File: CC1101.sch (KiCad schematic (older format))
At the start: 30 parts, among them J201 Conn_Coaxial, U201 CC1101RGPR, Y201 26MHz

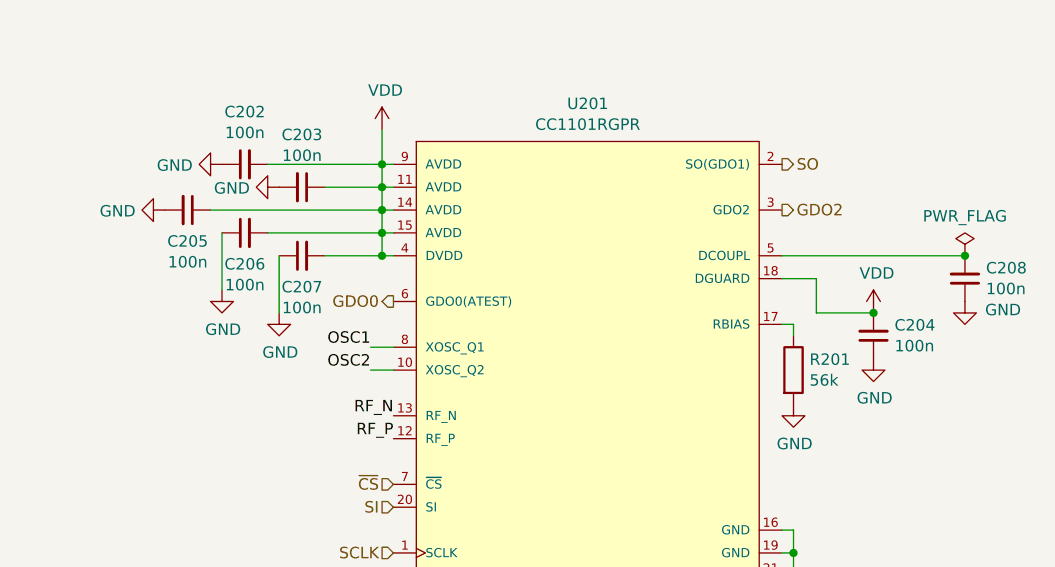
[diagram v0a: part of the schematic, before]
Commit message: select more JLC components
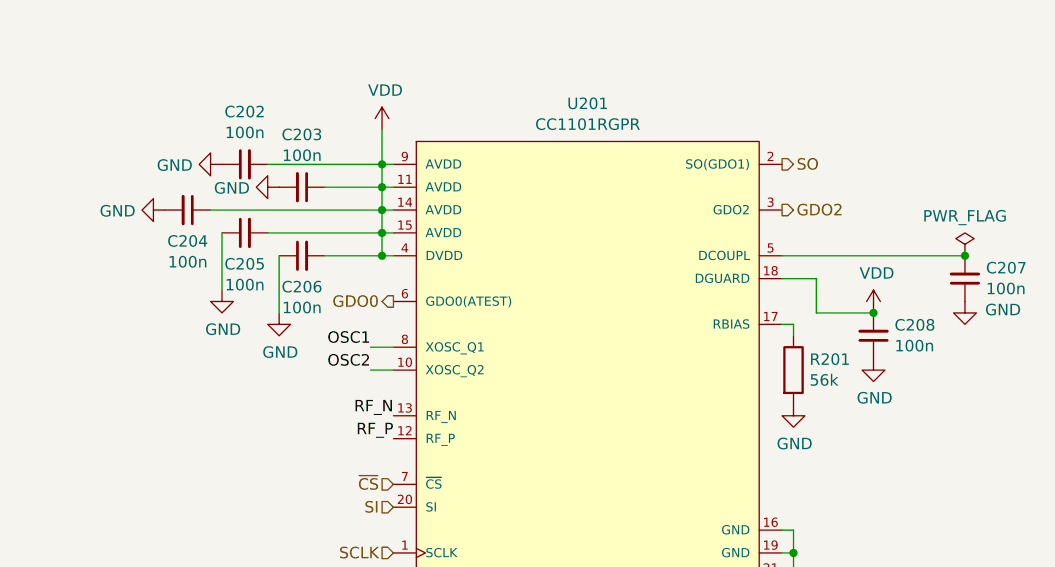
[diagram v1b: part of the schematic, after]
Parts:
- C211: LCSC (none) -> C1546; Type (none) -> FH 0402CG101J500NT
- C212, C217: LCSC (none) -> C1552; Type (none) -> FH 0402CG1R5C500NT
- C213: LCSC (none) -> C1547; Type (none) -> FH 0402CG120J500NT
- C214: footprint Capacitor_SMD:C_0402_1005Metric -> Capacitor_SMD:C_0603_1608Metric; LCSC (none) -> C1567; Type (none) -> FH 0402CG470J500NT
- C215: LCSC (none) -> C1550; Type (none) -> FH 0402CG1R0C500NT
- C216: LCSC (none) -> C1565; Type (none) -> FH 0402CG3R3C500NT
- FB201: Param Single basic one at JLC -> Only basic one at JLC
- L201, L207: LCSC (none) -> C24562; Type (none) -> Sunlord SDCL1005C18NJTDF
- L202, L203, L204, L206: LCSC (none) -> C24563; Type (none) -> Sunlord SDCL1005C12NJTDF
- renumbered C205 to C204, C206 to C205, C207 to C206, C208 to C207, C204 to C208

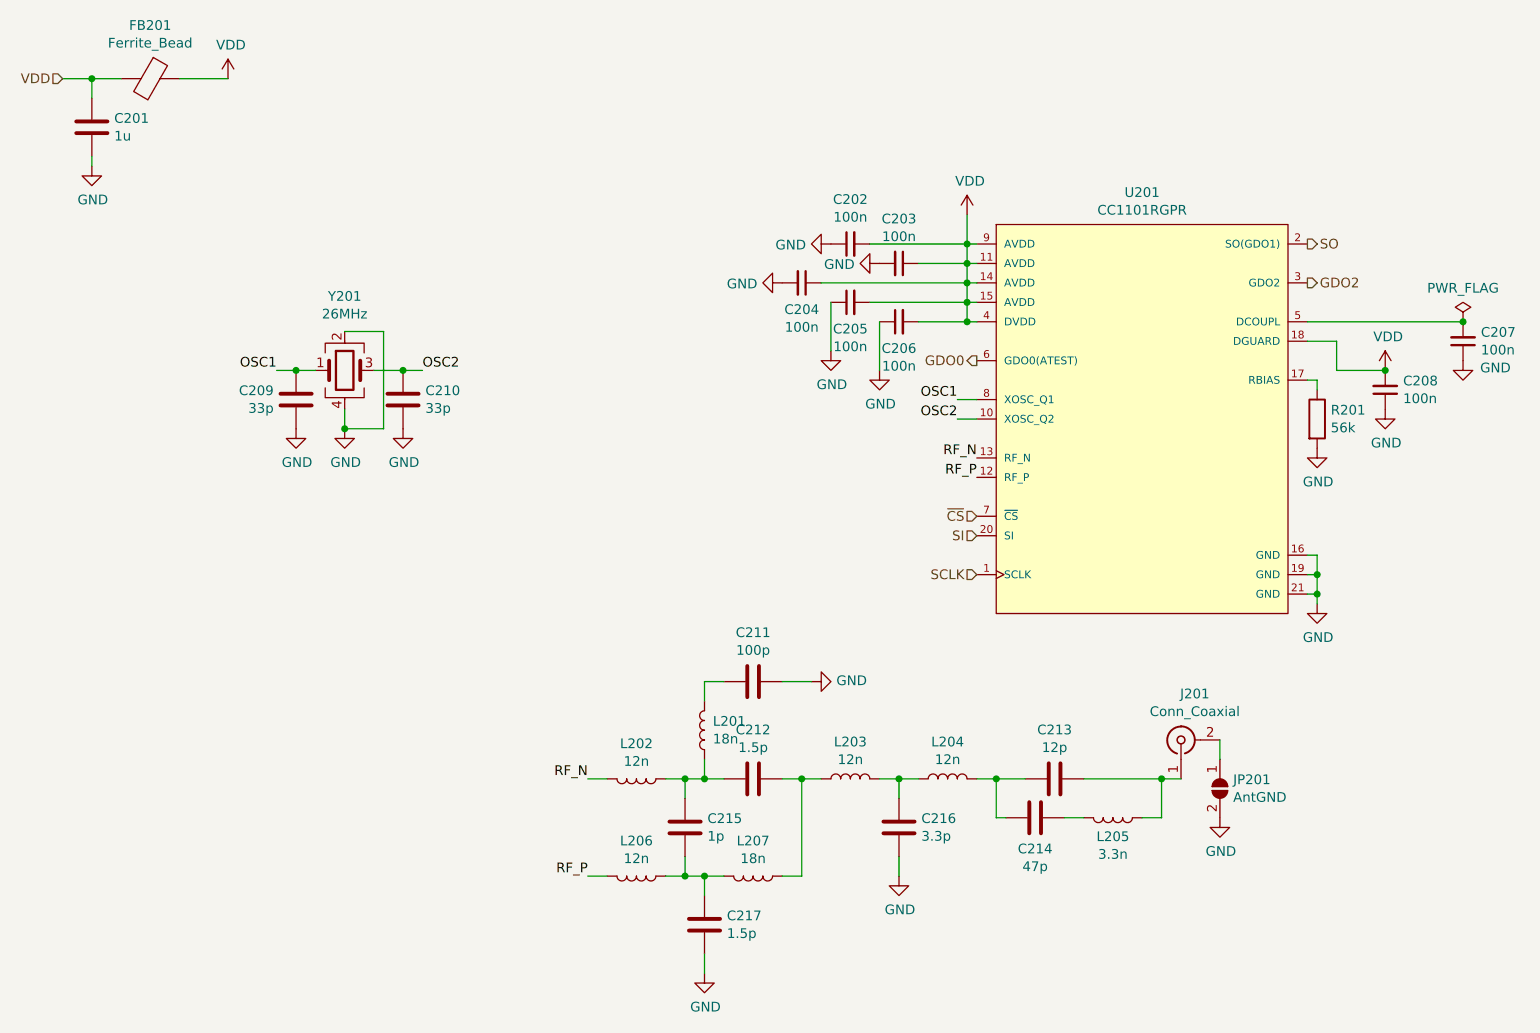
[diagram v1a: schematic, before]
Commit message: raw component placement
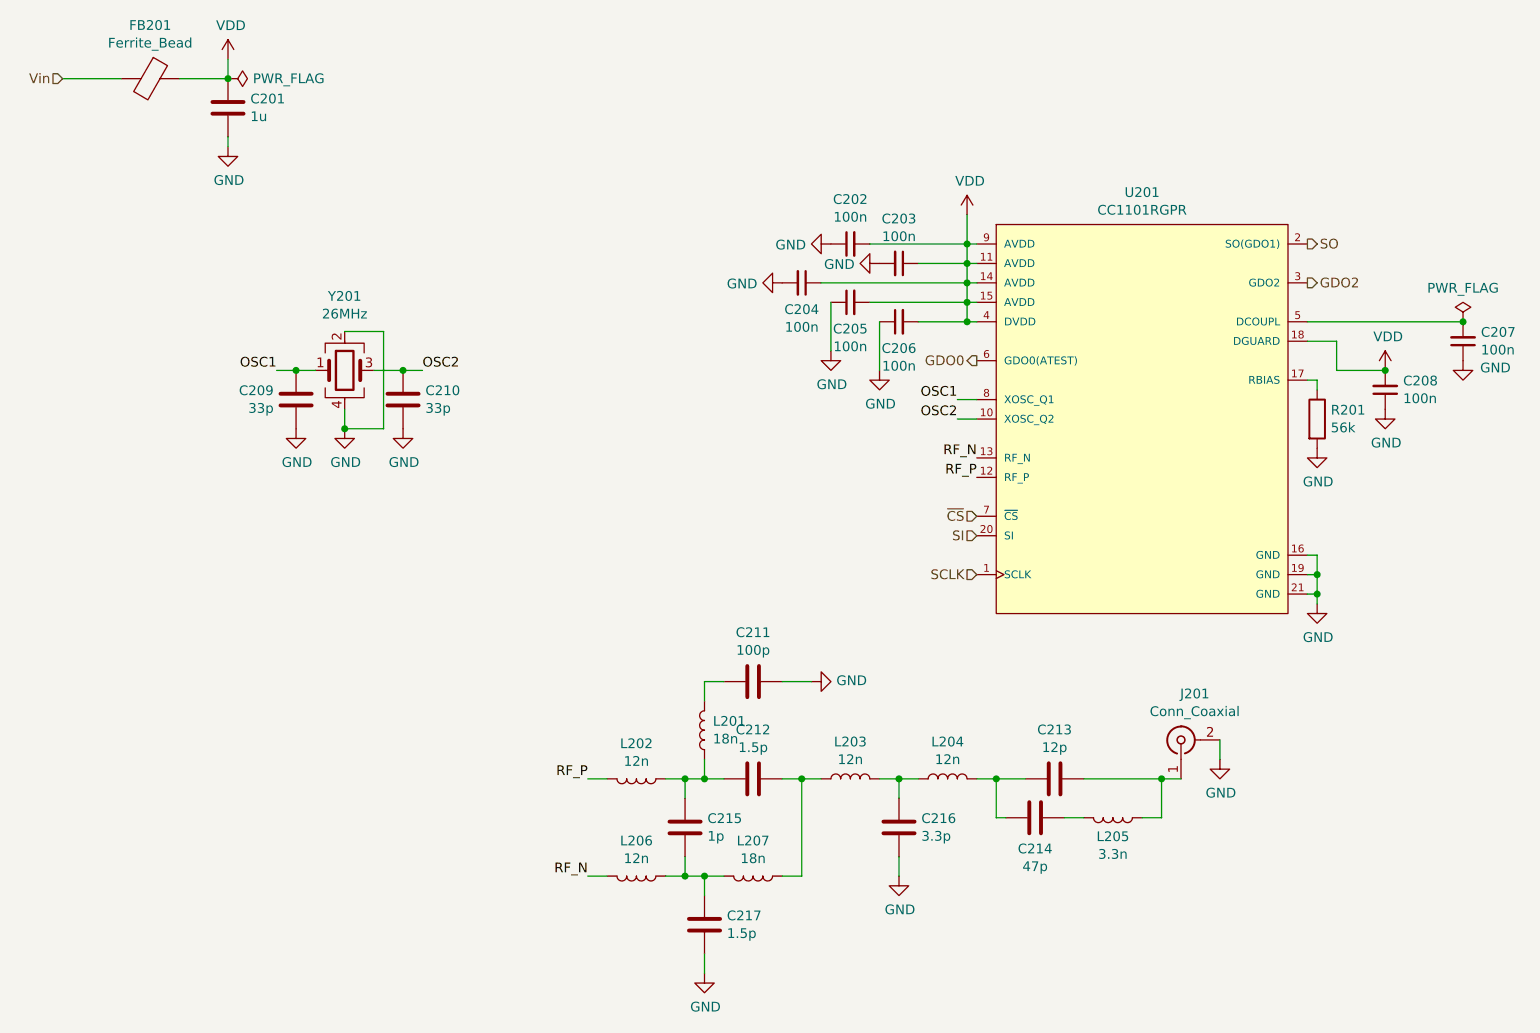
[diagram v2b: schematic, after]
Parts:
- removed JP201: AntGND, Jumper:SolderJumper-2_P1.3mm_Open_RoundedPad1.0x1.5mm, symbol Jumper:SolderJumper_2_Open
- C214: footprint Capacitor_SMD:C_0603_1608Metric -> Capacitor_SMD:C_0402_1005Metric
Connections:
- net GND: now also J201.2 (Ext)
- net RF_N: now also L206.2; no longer L202.2
- net RF_P: now also L202.2; no longer L206.2
- net VDD: no longer FB201.2
- new net Vin: FB201.2
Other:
- moved on the sheet: C201
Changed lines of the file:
@@
 GDO0
 Text HLabel 700  900  0    50   Input ~ 0
-VDD
+Vin
 $Comp
 L Device:C_Small C205
@@
 L power:VDD #PWR0201
 U 1 1 6086AF52
-P 1550 900
-F 0 "#PWR0201" H 1550 750 50  0001 C CNN
-F 1 "VDD" H 1565 1073 50  0000 C CNN
-F 2 "" H 1550 900 50  0001 C CNN
-F 3 "" H 1550 900 50  0001 C CNN
-	1    1550 900
+P 1550 800
+F 0 "#PWR0201" H 1550 650 50  0001 C CNN
+F 1 "VDD" H 1565 973 50  0000 C CNN
+F 2 "" H 1550 800 50  0001 C CNN
+F 3 "" H 1550 800 50  0001 C CNN
+	1    1550 800
 	1    0    0    -1
 $EndComp
@@
 	0    1    1    0
 $EndComp
-Wire Wire Line
-	1550 900  1300 900
 $Comp
 L Device:C C201
 U 1 1 6086D468
-P 850 1150
-F 0 "C201" H 965 1196 50  0000 L CNN
-F 1 "1u" H 965 1105 50  0000 L CNN
-F 2 "Capacitor_SMD:C_0805_2012Metric" H 888 1000 50  0001 C CNN
-F 3 "https://datasheet.lcsc.com/lcsc/1810191216_Samsung-Electro-Mechanics-CL21B105KBFNNNE_C28323.pdf" H 850 1150 50  0001 C CNN
-F 4 "Samsung CL21B105KBFNNNE" H 850 1150 50  0001 C CNN "Type"
-F 5 "C28323" H 850 1150 50  0001 C CNN "LCSC"
-F 6 "X7R" H 850 1150 50  0001 C CNN "Param"
-	1    850  1150
-	1    0    0    -1
-$EndComp
-Wire Wire Line
-	700  900  850  900
-Wire Wire Line
-	850  1000 850  900
-Connection ~ 850  900
-Wire Wire Line
-	850  900  1000 900
+P 1550 1050
+F 0 "C201" H 1665 1096 50  0000 L CNN
+F 1 "1u" H 1665 1005 50  0000 L CNN
+F 2 "Capacitor_SMD:C_0805_2012Metric" H 1588 900 50  0001 C CNN
+F 3 "https://datasheet.lcsc.com/lcsc/1810191216_Samsung-Electro-Mechanics-CL21B105KBFNNNE_C28323.pdf" H 1550 1050 50  0001 C CNN
+F 4 "Samsung CL21B105KBFNNNE" H 1550 1050 50  0001 C CNN "Type"
+F 5 "C28323" H 1550 1050 50  0001 C CNN "LCSC"
+F 6 "X7R" H 1550 1050 50  0001 C CNN "Param"
+	1    1550 1050
+	1    0    0    -1
+$EndComp
 $Comp
 L power:GND #PWR0202
 U 1 1 6086EAEC
-P 850 1350
-F 0 "#PWR0202" H 850 1100 50  0001 C CNN
-F 1 "GND" H 855 1177 50  0000 C CNN
-F 2 "" H 850 1350 50  0001 C CNN
-F 3 "" H 850 1350 50  0001 C CNN
-	1    850  1350
-	1    0    0    -1
-$EndComp
-Wire Wire Line
-	850  1350 850  1300
+P 1550 1250
+F 0 "#PWR0202" H 1550 1000 50  0001 C CNN
+F 1 "GND" H 1555 1077 50  0000 C CNN
+F 2 "" H 1550 1250 50  0001 C CNN
+F 3 "" H 1550 1250 50  0001 C CNN
+	1    1550 1250
+	1    0    0    -1
+$EndComp
+Wire Wire Line
+	1550 1250 1550 1200
+Text Label 3400 5000 2    50   ~ 0
+RF_N
 Text Label 3400 4500 2    50   ~ 0
-RF_N
-Text Label 3400 5000 2    50   ~ 0
 RF_P
 $Comp
@@
 F 0 "C214" V 5860 4700 50  0000 C CNN
 F 1 "47p" V 5951 4700 50  0000 C CNN
-F 2 "Capacitor_SMD:C_0603_1608Metric" H 5738 4550 50  0001 C CNN
+F 2 "Capacitor_SMD:C_0402_1005Metric" H 5738 4550 50  0001 C CNN
 F 3 "https://datasheet.lcsc.com/szlcsc/Guangdong-Fenghua-Advanced-Tech-0402CG470J500NT_C1567.pdf" H 5700 4700 50  0001 C CNN
 F 4 "" V 5700 4700 50  0001 C CNN "type"
@@
 	6650 4300 6650 4400
 $Comp
-L power:GND #PWR0218
-U 1 1 608ABD9C
-P 6650 4700
-F 0 "#PWR0218" H 6650 4450 50  0001 C CNN
-F 1 "GND" H 6655 4527 50  0000 C CNN
-F 2 "" H 6650 4700 50  0001 C CNN
-F 3 "" H 6650 4700 50  0001 C CNN
-	1    6650 4700
-	1    0    0    -1
-$EndComp
-$Comp
-L Jumper:SolderJumper_2_Open JP201
-U 1 1 608E6674
-P 6650 4550
-F 0 "JP201" V 6604 4618 50  0000 L CNN
-F 1 "AntGND" V 6695 4618 50  0000 L CNN
-F 2 "Jumper:SolderJumper-2_P1.3mm_Open_RoundedPad1.0x1.5mm" H 6650 4550 50  0001 C CNN
-F 3 "~" H 6650 4550 50  0001 C CNN
-F 4 "0" H 6650 4550 50  0001 C CNN "JLCPCB BOM"
-	1    6650 4550
-	0    1    1    0
-$EndComp
-$Comp
 L power:GND #PWR0220
 U 1 1 608E70BF
@@
 	7250 2400 7500 2400
 Connection ~ 7500 2400
+$Comp
+L power:GND #PWR0218
+U 1 1 608ABD9C
+P 6650 4400
+F 0 "#PWR0218" H 6650 4150 50  0001 C CNN
+F 1 "GND" H 6655 4227 50  0000 C CNN
+F 2 "" H 6650 4400 50  0001 C CNN
+F 3 "" H 6650 4400 50  0001 C CNN
+	1    6650 4400
+	1    0    0    -1
+$EndComp
+Wire Wire Line
+	700  900  1000 900
+$Comp
+L power:PWR_FLAG #FLG0103
+U 1 1 608E32C9
+P 1550 900
+F 0 "#FLG0103" H 1550 975 50  0001 C CNN
+F 1 "PWR_FLAG" V 1550 1028 50  0000 L CNN
+F 2 "" H 1550 900 50  0001 C CNN
+F 3 "~" H 1550 900 50  0001 C CNN
+	1    1550 900
+	0    1    1    0
+$EndComp
+Connection ~ 1550 900
+Wire Wire Line
+	1300 900  1550 900
+Wire Wire Line
+	1550 900  1550 800
 $EndSCHEMATC

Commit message: place CC1101 circuits
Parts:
- J201: footprint Connector_Coaxial:SMA_Molex_73251-1153_EdgeMount_Horizontal -> Connector_Coaxial:SMA_Amphenol_901-144_Vertical
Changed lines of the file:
@@
 F 0 "J201" V 6687 4229 50  0000 C CNN
 F 1 "Conn_Coaxial" V 6596 4229 50  0000 C CNN
-F 2 "Connector_Coaxial:SMA_Molex_73251-1153_EdgeMount_Horizontal" H 6450 4300 50  0001 C CNN
+F 2 "Connector_Coaxial:SMA_Amphenol_901-144_Vertical" H 6450 4300 50  0001 C CNN
 F 3 " ~" H 6450 4300 50  0001 C CNN
 F 4 "0" H 6450 4300 50  0001 C CNN "JLCPCB BOM"
